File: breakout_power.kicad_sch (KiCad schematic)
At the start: 6 parts, among them U23 AP2112K-1.8, U3 AP2112K-3.3TRG1

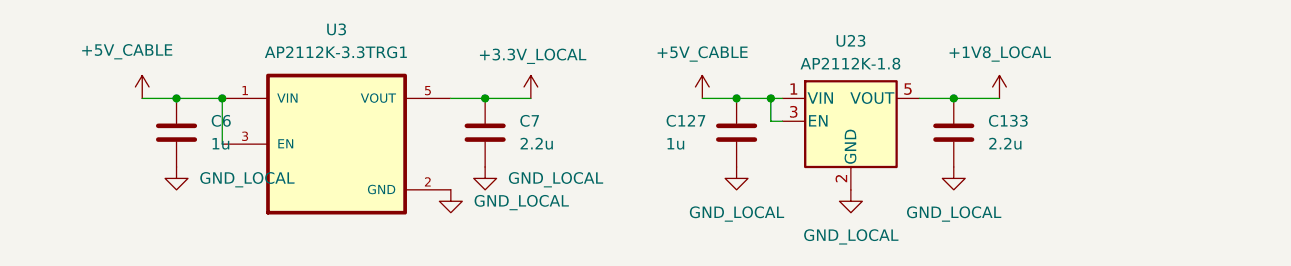
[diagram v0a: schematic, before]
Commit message: Fixed most ERC checks
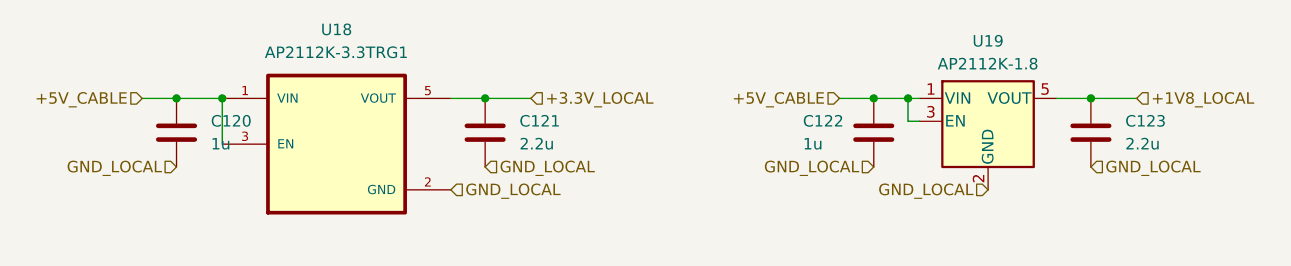
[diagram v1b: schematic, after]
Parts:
- renumbered C6 to C120, C7 to C121, C127 to C122, C133 to C123, U3 to U18, U23 to U19
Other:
- moved on the sheet: C122, C123, U19

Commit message: Footprinting done (warnings on schematic side but pcb import works fine)
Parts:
- C120, C121, C123: footprint (none) -> Capacitor_SMD:C_0603_1608Metric
- C122: footprint (none) -> Inductor_SMD:IND-SMD_L10.4-W10.3
- U18: symbol AD_2112K-1.8:AP2112K-3.3TRG1 -> AP_2112K-1.8:AP2112K-3.3TRG1
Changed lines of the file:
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@@
 			)
 		)
-		(property "Footprint" ""
+		(property "Footprint" "Capacitor_SMD:C_0603_1608Metric"
 			(at 142.5448 49.53 0)
 			(effects
@@
 			)
 		)
-		(property "Footprint" ""
+		(property "Footprint" "Inductor_SMD:IND-SMD_L10.4-W10.3"
 			(at 120.3452 57.15 0)
 			(effects
@@
 	)
 	(symbol
-		(lib_id "AD_2112K-1.8:AP2112K-3.3TRG1")
+		(lib_id "AP_2112K-1.8:AP2112K-3.3TRG1")
 		(at 59.69 54.61 0)
 		(unit 1)
@@
 		)
 		(pin "3"
+		)
+		(pin "4"
 		)
 		(instances
@@
 			)
 		)
-		(property "Footprint" ""
+		(property "Footprint" "Capacitor_SMD:C_0603_1608Metric"
 			(at 42.8752 57.15 0)
 			(effects
@@
 			)
 		)
-		(property "Footprint" ""
+		(property "Footprint" "Capacitor_SMD:C_0603_1608Metric"
 			(at 75.2348 49.53 0)
 			(effects

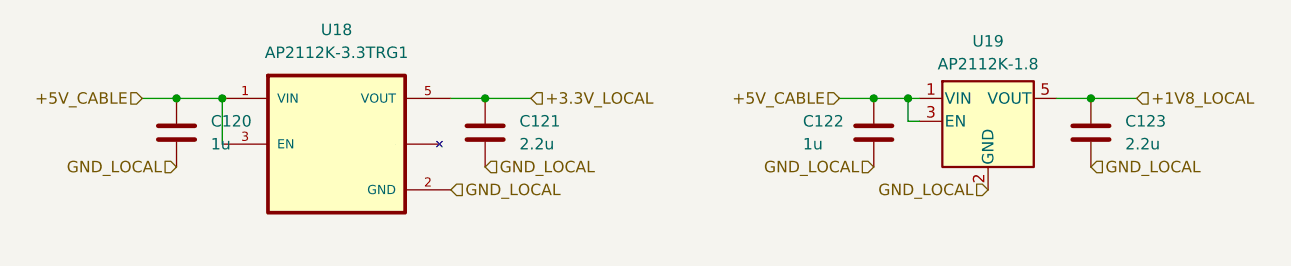
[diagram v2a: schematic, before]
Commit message: Minor schematic changes
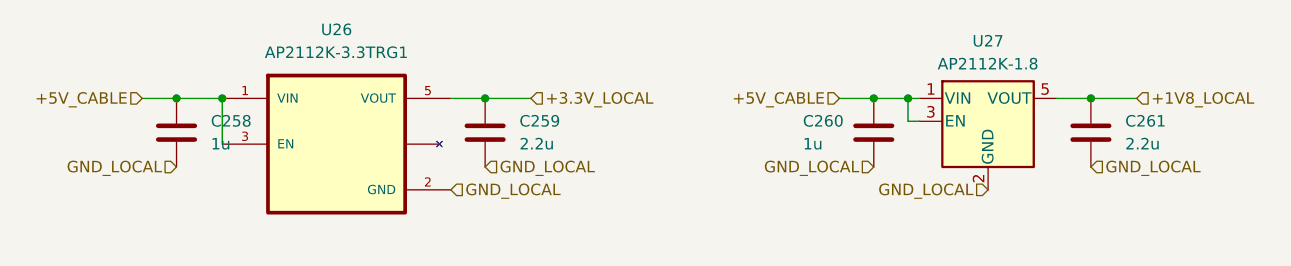
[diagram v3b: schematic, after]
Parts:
- C258: renamed from C120; LCSC Part # (none) -> C15849
- C259: renamed from C121; LCSC Part # (none) -> C23630
- C260: renamed from C122; LCSC Part # (none) -> C15849
- C261: renamed from C123; LCSC Part # (none) -> C23630
- renumbered U18 to U26, U19 to U27
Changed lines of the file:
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@@
 		(dnp no)
 		(fields_autoplaced yes)
-		(property "Reference" "C123"
+		(property "Reference" "C261"
 			(at 147.32 52.0699 0)
 			(effects
@@
 		)
 		(property "Description" "Unpolarized capacitor"
+			(at 143.51 53.34 0)
+			(effects
+				(font
+					(size 1.27 1.27)
+				)
+				(hide yes)
+			)
+		)
+		(property "LCSC Part #" "C23630"
 			(at 143.51 53.34 0)
 			(effects
@@
 			(project "AEC_Speaker_Mic_System"
 				(path "/b4ee80b5-9d9a-4551-9b0c-6a8cb8d78ca3/1f359754-8963-4278-b0fc-0e057045f0f0/09f4d9e7-7b98-4823-896d-27be6c165bee"
-					(reference "C138")
+					(reference "C285")
 					(unit 1)
 				)
 				(path "/b4ee80b5-9d9a-4551-9b0c-6a8cb8d78ca3/53a31f69-3ae8-42c4-b16b-bf4423ba2408/09f4d9e7-7b98-4823-896d-27be6c165bee"
-					(reference "C123")
+					(reference "C261")
 					(unit 1)
 				)
 				(path "/b4ee80b5-9d9a-4551-9b0c-6a8cb8d78ca3/5b6bff76-1c00-4ff8-b189-bd0a46683e6a/09f4d9e7-7b98-4823-896d-27be6c165bee"
-					(reference "C144")
+					(reference "C296")
 					(unit 1)
 				)
 				(path "/b4ee80b5-9d9a-4551-9b0c-6a8cb8d78ca3/89a51368-2ba7-4a3f-afe3-5d1fde30878e/09f4d9e7-7b98-4823-896d-27be6c165bee"
-					(reference "C149")
+					(reference "C304")
 					(unit 1)
 				)
 				(path "/b4ee80b5-9d9a-4551-9b0c-6a8cb8d78ca3/a283a138-17fa-468a-9410-2c24c1f3e11b/09f4d9e7-7b98-4823-896d-27be6c165bee"
-					(reference "C133")
+					(reference "C277")
 					(unit 1)
 				)
 				(path "/b4ee80b5-9d9a-4551-9b0c-6a8cb8d78ca3/b49b60b2-4846-4243-abe7-f73c4650f1e7/09f4d9e7-7b98-4823-896d-27be6c165bee"
-					(reference "C128")
+					(reference "C268")
 					(unit 1)
 				)
@@
 		(dnp no)
 		(fields_autoplaced yes)
-		(property "Reference" "U19"
+		(property "Reference" "U27"
 			(at 132.08 43.18 0)
 			(effects
@@
 			(project ""
 				(path "/b4ee80b5-9d9a-4551-9b0c-6a8cb8d78ca3/1f359754-8963-4278-b0fc-0e057045f0f0/09f4d9e7-7b98-4823-896d-27be6c165bee"
-					(reference "U37")
+					(reference "U48")
 					(unit 1)
 				)
 				(path "/b4ee80b5-9d9a-4551-9b0c-6a8cb8d78ca3/53a31f69-3ae8-42c4-b16b-bf4423ba2408/09f4d9e7-7b98-4823-896d-27be6c165bee"
-					(reference "U19")
+					(reference "U27")
 					(unit 1)
 				)
 				(path "/b4ee80b5-9d9a-4551-9b0c-6a8cb8d78ca3/5b6bff76-1c00-4ff8-b189-bd0a46683e6a/09f4d9e7-7b98-4823-896d-27be6c165bee"
-					(reference "U44")
+					(reference "U56")
 					(unit 1)
 				)
 				(path "/b4ee80b5-9d9a-4551-9b0c-6a8cb8d78ca3/89a51368-2ba7-4a3f-afe3-5d1fde30878e/09f4d9e7-7b98-4823-896d-27be6c165bee"
-					(reference "U50")
+					(reference "U63")
 					(unit 1)
 				)
 				(path "/b4ee80b5-9d9a-4551-9b0c-6a8cb8d78ca3/a283a138-17fa-468a-9410-2c24c1f3e11b/09f4d9e7-7b98-4823-896d-27be6c165bee"
-					(reference "U31")
+					(reference "U41")
 					(unit 1)
 				)
 				(path "/b4ee80b5-9d9a-4551-9b0c-6a8cb8d78ca3/b49b60b2-4846-4243-abe7-f73c4650f1e7/09f4d9e7-7b98-4823-896d-27be6c165bee"
-					(reference "U22")
+					(reference "U30")
 					(unit 1)
 				)
@@
 		(on_board yes)
 		(dnp no)
-		(property "Reference" "C122"
+		(property "Reference" "C260"
 			(at 111.506 52.07 0)
 			(effects
@@
 		)
 		(property "Description" "Unpolarized capacitor"
+			(at 119.38 53.34 0)
+			(effects
+				(font
+					(size 1.27 1.27)
+				)
+				(hide yes)
+			)
+		)
+		(property "LCSC Part #" "C15849"
 			(at 119.38 53.34 0)
 			(effects
@@
 			(project "AEC_Speaker_Mic_System"
 				(path "/b4ee80b5-9d9a-4551-9b0c-6a8cb8d78ca3/1f359754-8963-4278-b0fc-0e057045f0f0/09f4d9e7-7b98-4823-896d-27be6c165bee"
-					(reference "C137")
+					(reference "C284")
 					(unit 1)
 				)
 				(path "/b4ee80b5-9d9a-4551-9b0c-6a8cb8d78ca3/53a31f69-3ae8-42c4-b16b-bf4423ba2408/09f4d9e7-7b98-4823-896d-27be6c165bee"
-					(reference "C122")
+					(reference "C260")
 					(unit 1)
 				)
 				(path "/b4ee80b5-9d9a-4551-9b0c-6a8cb8d78ca3/5b6bff76-1c00-4ff8-b189-bd0a46683e6a/09f4d9e7-7b98-4823-896d-27be6c165bee"
-					(reference "C143")
+					(reference "C295")
 					(unit 1)
 				)
 				(path "/b4ee80b5-9d9a-4551-9b0c-6a8cb8d78ca3/89a51368-2ba7-4a3f-afe3-5d1fde30878e/09f4d9e7-7b98-4823-896d-27be6c165bee"
-					(reference "C148")
+					(reference "C303")
 					(unit 1)
 				)
 				(path "/b4ee80b5-9d9a-4551-9b0c-6a8cb8d78ca3/a283a138-17fa-468a-9410-2c24c1f3e11b/09f4d9e7-7b98-4823-896d-27be6c165bee"
-					(reference "C132")
+					(reference "C276")
 					(unit 1)
 				)
 				(path "/b4ee80b5-9d9a-4551-9b0c-6a8cb8d78ca3/b49b60b2-4846-4243-abe7-f73c4650f1e7/09f4d9e7-7b98-4823-896d-27be6c165bee"
-					(reference "C127")
+					(reference "C267")
 					(unit 1)
 				)
@@
 		(dnp no)
 		(fields_autoplaced yes)
-		(property "Reference" "U18"
+		(property "Reference" "U26"
 			(at 59.69 41.91 0)
 			(effects
@@
 			(project "AEC_Speaker_Mic_System"
 				(path "/b4ee80b5-9d9a-4551-9b0c-6a8cb8d78ca3/1f359754-8963-4278-b0fc-0e057045f0f0/09f4d9e7-7b98-4823-896d-27be6c165bee"
-					(reference "U36")
+					(reference "U47")
 					(unit 1)
 				)
 				(path "/b4ee80b5-9d9a-4551-9b0c-6a8cb8d78ca3/53a31f69-3ae8-42c4-b16b-bf4423ba2408/09f4d9e7-7b98-4823-896d-27be6c165bee"
-					(reference "U18")
+					(reference "U26")
 					(unit 1)
 				)
 				(path "/b4ee80b5-9d9a-4551-9b0c-6a8cb8d78ca3/5b6bff76-1c00-4ff8-b189-bd0a46683e6a/09f4d9e7-7b98-4823-896d-27be6c165bee"
-					(reference "U43")
+					(reference "U55")
 					(unit 1)
 				)
 				(path "/b4ee80b5-9d9a-4551-9b0c-6a8cb8d78ca3/89a51368-2ba7-4a3f-afe3-5d1fde30878e/09f4d9e7-7b98-4823-896d-27be6c165bee"
-					(reference "U49")
+					(reference "U62")
 					(unit 1)
 				)
 				(path "/b4ee80b5-9d9a-4551-9b0c-6a8cb8d78ca3/a283a138-17fa-468a-9410-2c24c1f3e11b/09f4d9e7-7b98-4823-896d-27be6c165bee"
-					(reference "U30")
+					(reference "U40")
 					(unit 1)
 				)
 				(path "/b4ee80b5-9d9a-4551-9b0c-6a8cb8d78ca3/b49b60b2-4846-4243-abe7-f73c4650f1e7/09f4d9e7-7b98-4823-896d-27be6c165bee"
-					(reference "U21")
+					(reference "U29")
 					(unit 1)
 				)
@@
 		(dnp no)
 		(fields_autoplaced yes)
-		(property "Reference" "C120"
+		(property "Reference" "C258"
 			(at 45.72 52.0699 0)
 			(effects
@@
 		)
 		(property "Description" "Unpolarized capacitor"
+			(at 41.91 53.34 0)
+			(effects
+				(font
+					(size 1.27 1.27)
+				)
+				(hide yes)
+			)
+		)
+		(property "LCSC Part #" "C15849"
 			(at 41.91 53.34 0)
 			(effects
@@
 			(project "AEC_Speaker_Mic_System"
 				(path "/b4ee80b5-9d9a-4551-9b0c-6a8cb8d78ca3/1f359754-8963-4278-b0fc-0e057045f0f0/09f4d9e7-7b98-4823-896d-27be6c165bee"
-					(reference "C135")
+					(reference "C282")
 					(unit 1)
 				)
 				(path "/b4ee80b5-9d9a-4551-9b0c-6a8cb8d78ca3/53a31f69-3ae8-42c4-b16b-bf4423ba2408/09f4d9e7-7b98-4823-896d-27be6c165bee"
-					(reference "C120")
+					(reference "C258")
 					(unit 1)
 				)
 				(path "/b4ee80b5-9d9a-4551-9b0c-6a8cb8d78ca3/5b6bff76-1c00-4ff8-b189-bd0a46683e6a/09f4d9e7-7b98-4823-896d-27be6c165bee"
-					(reference "C141")
+					(reference "C293")
 					(unit 1)
 				)
 				(path "/b4ee80b5-9d9a-4551-9b0c-6a8cb8d78ca3/89a51368-2ba7-4a3f-afe3-5d1fde30878e/09f4d9e7-7b98-4823-896d-27be6c165bee"
-					(reference "C146")
+					(reference "C301")
 					(unit 1)
 				)
 				(path "/b4ee80b5-9d9a-4551-9b0c-6a8cb8d78ca3/a283a138-17fa-468a-9410-2c24c1f3e11b/09f4d9e7-7b98-4823-896d-27be6c165bee"
-					(reference "C130")
+					(reference "C274")
 					(unit 1)
 				)
 				(path "/b4ee80b5-9d9a-4551-9b0c-6a8cb8d78ca3/b49b60b2-4846-4243-abe7-f73c4650f1e7/09f4d9e7-7b98-4823-896d-27be6c165bee"
-					(reference "C125")
+					(reference "C265")
 					(unit 1)
 				)
@@
 		(dnp no)
 		(fields_autoplaced yes)
-		(property "Reference" "C121"
+		(property "Reference" "C259"
 			(at 80.01 52.0699 0)
 			(effects
@@
 		)
 		(property "Description" "Unpolarized capacitor"
+			(at 76.2 53.34 0)
+			(effects
+				(font
+					(size 1.27 1.27)
+				)
+				(hide yes)
+			)
+		)
+		(property "LCSC Part #" "C23630"
 			(at 76.2 53.34 0)
 			(effects
@@
 			(project "AEC_Speaker_Mic_System"
 				(path "/b4ee80b5-9d9a-4551-9b0c-6a8cb8d78ca3/1f359754-8963-4278-b0fc-0e057045f0f0/09f4d9e7-7b98-4823-896d-27be6c165bee"
-					(reference "C136")
+					(reference "C283")
 					(unit 1)
 				)
 				(path "/b4ee80b5-9d9a-4551-9b0c-6a8cb8d78ca3/53a31f69-3ae8-42c4-b16b-bf4423ba2408/09f4d9e7-7b98-4823-896d-27be6c165bee"
-					(reference "C121")
+					(reference "C259")
 					(unit 1)
 				)
 				(path "/b4ee80b5-9d9a-4551-9b0c-6a8cb8d78ca3/5b6bff76-1c00-4ff8-b189-bd0a46683e6a/09f4d9e7-7b98-4823-896d-27be6c165bee"
-					(reference "C142")
+					(reference "C294")
 					(unit 1)
 				)
 				(path "/b4ee80b5-9d9a-4551-9b0c-6a8cb8d78ca3/89a51368-2ba7-4a3f-afe3-5d1fde30878e/09f4d9e7-7b98-4823-896d-27be6c165bee"
-					(reference "C147")
+					(reference "C302")
 					(unit 1)
 				)
 				(path "/b4ee80b5-9d9a-4551-9b0c-6a8cb8d78ca3/a283a138-17fa-468a-9410-2c24c1f3e11b/09f4d9e7-7b98-4823-896d-27be6c165bee"
-					(reference "C131")
+					(reference "C275")
 					(unit 1)
 				)
 				(path "/b4ee80b5-9d9a-4551-9b0c-6a8cb8d78ca3/b49b60b2-4846-4243-abe7-f73c4650f1e7/09f4d9e7-7b98-4823-896d-27be6c165bee"
-					(reference "C126")
-					(unit 1)
-				)
+					(reference "C266")
+					(unit 1)
+				)
